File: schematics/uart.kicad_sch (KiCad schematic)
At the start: 8 parts, among them J8 myBus, U8 74HC238, U9 W65C51N, X1 CXO_DIP8

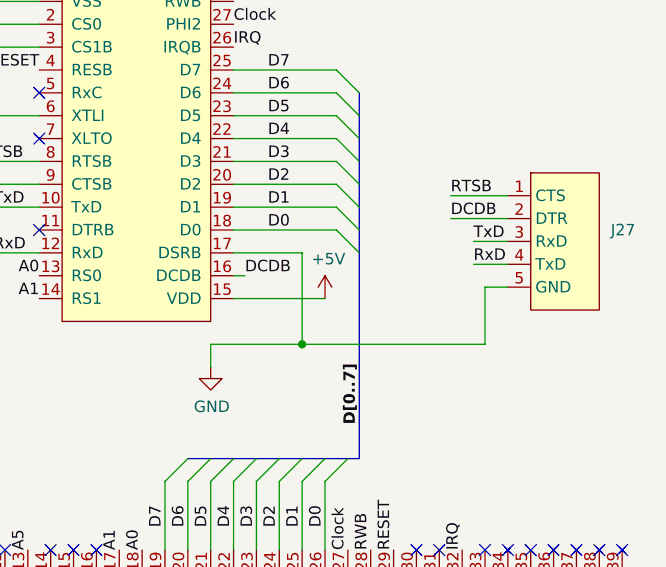
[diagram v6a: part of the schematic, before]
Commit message: new UART support
fix schematics by adding a resistor
renaming PC/2 to correct PS/2
Updating FORTH to detect terminal connection
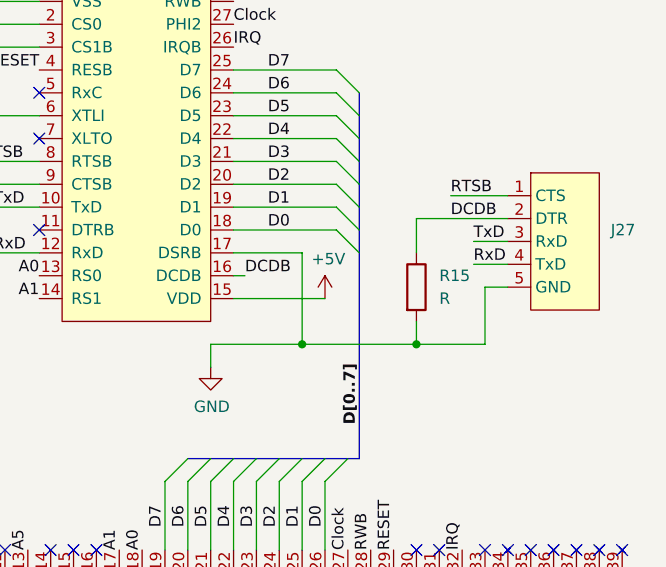
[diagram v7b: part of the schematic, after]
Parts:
- added R15: R, symbol Device:R
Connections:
- net DCDB: now also R15.1
- net GND: now also R15.2
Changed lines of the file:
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@@
+	)
+	(junction
+		(at 162.56 115.57)
+		(diameter 0)
+		(color 0 0 0 0)
 	)
 	(junction
@@
 		)
 	)
+	(wire
+		(pts
+			(xy 162.56 113.03) (xy 162.56 115.57)
+		)
+		(stroke
+			(width 0)
+			(type default)
+		)
+	)
 	(bus
 		(pts
@@
 	(wire
 		(pts
+			(xy 162.56 115.57) (xy 170.18 115.57)
+		)
+		(stroke
+			(width 0)
+			(type default)
+		)
+	)
+	(wire
+		(pts
 			(xy 142.24 100.33) (xy 153.67 100.33)
 		)
@@
 	(wire
 		(pts
+			(xy 162.56 101.6) (xy 172.72 101.6)
+		)
+		(stroke
+			(width 0)
+			(type default)
+		)
+	)
+	(wire
+		(pts
 			(xy 107.95 64.77) (xy 111.76 64.77)
 		)
@@
 	(wire
 		(pts
+			(xy 162.56 105.41) (xy 162.56 101.6)
+		)
+		(stroke
+			(width 0)
+			(type default)
+		)
+	)
+	(wire
+		(pts
 			(xy 100.33 105.41) (xy 100.33 100.33)
 		)
@@
 	(wire
 		(pts
-			(xy 166.37 101.6) (xy 172.72 101.6)
-		)
-		(stroke
-			(width 0)
-			(type default)
-		)
-	)
-	(wire
-		(pts
 			(xy 142.24 87.63) (xy 153.67 87.63)
 		)
@@
 	(wire
 		(pts
-			(xy 149.86 115.57) (xy 170.18 115.57)
+			(xy 149.86 115.57) (xy 162.56 115.57)
 		)
 		(stroke
@@
 					(unit 1)
 				)
+			)
+		)
+	)
+	(symbol
+		(lib_id "Device:R")
+		(at 162.56 109.22 0)
+		(unit 1)
+		(exclude_from_sim no)
+		(in_bom yes)
+		(on_board yes)
+		(dnp no)
+		(fields_autoplaced yes)
+		(property "Reference" "R15"
+			(at 165.1 107.9499 0)
+			(effects
+				(font
+					(size 1.27 1.27)
+				)
+				(justify left)
+			)
+		)
+		(property "Value" "R"
+			(at 165.1 110.4899 0)
+			(effects
+				(font
+					(size 1.27 1.27)
+				)
+				(justify left)
+			)
+		)
+		(property "Footprint" ""
+			(at 160.782 109.22 90)
+			(effects
+				(font
+					(size 1.27 1.27)
+				)
+				(hide yes)
+			)
+		)
+		(property "Datasheet" "~"
+			(at 162.56 109.22 0)
+			(effects
+				(font
+					(size 1.27 1.27)
+				)
+				(hide yes)
+			)
+		)
+		(property "Description" "Resistor"
+			(at 162.56 109.22 0)
+			(effects
+				(font
+					(size 1.27 1.27)
+				)
+				(hide yes)
+			)
+		)
+		(pin "2"
+		)
+		(pin "1"
+		)
+		(instances
+			(project ""
+				(path "/03a78ca6-eaff-4f05-be7b-36cd15f8b56d/e1937880-b4d5-4732-8378-398cc9358f14"
+					(reference "R15")
+					(unit 1)
+				)

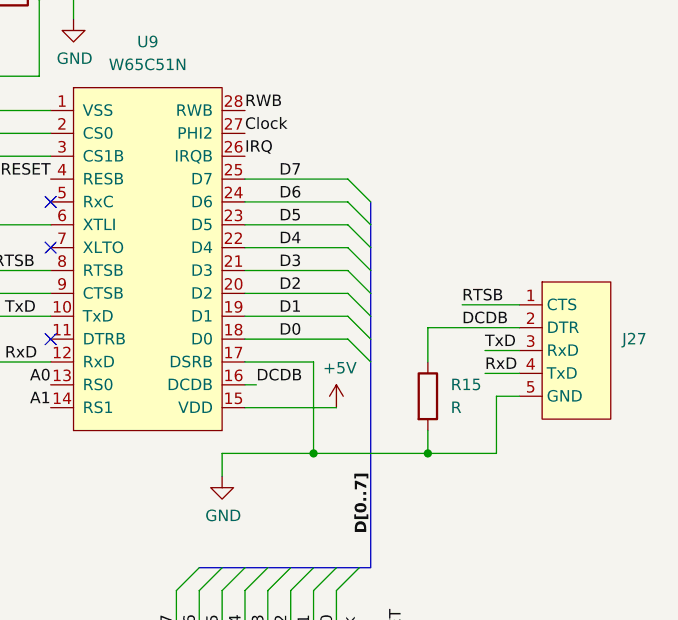
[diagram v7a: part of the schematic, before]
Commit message: Fix UART pullup
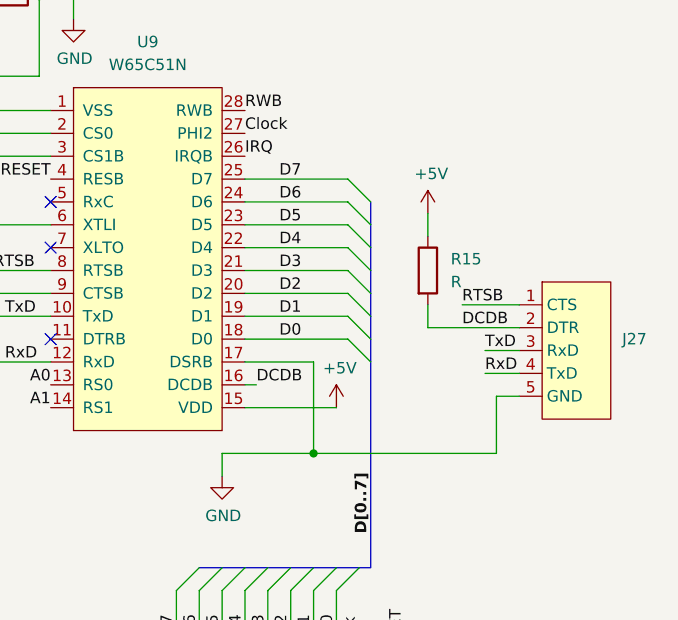
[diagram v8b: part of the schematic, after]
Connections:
- net +5V: now also R15.1
- net DCDB: now also R15.2; no longer R15.1
- net GND: no longer R15.2
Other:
- moved on the sheet: R15
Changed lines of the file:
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@@
-	)
-	(junction
-		(at 162.56 115.57)
-		(diameter 0)
-		(color 0 0 0 0)
 	)
 	(junction
@@
 		)
 	)
-	(wire
-		(pts
-			(xy 162.56 113.03) (xy 162.56 115.57)
-		)
-		(stroke
-			(width 0)
-			(type default)
-		)
-	)
 	(bus
 		(pts
@@
 	(wire
 		(pts
-			(xy 162.56 115.57) (xy 170.18 115.57)
+			(xy 149.86 115.57) (xy 170.18 115.57)
 		)
 		(stroke
@@
 	(wire
 		(pts
+			(xy 162.56 99.06) (xy 162.56 101.6)
+		)
+		(stroke
+			(width 0)
+			(type default)
+		)
+	)
+	(wire
+		(pts
 			(xy 113.03 82.55) (xy 120.65 82.55)
 		)
@@
 	(wire
 		(pts
+			(xy 162.56 88.9) (xy 162.56 91.44)
+		)
+		(stroke
+			(width 0)
+			(type default)
+		)
+	)
+	(wire
+		(pts
 			(xy 107.95 64.77) (xy 111.76 64.77)
 		)
@@
 	(wire
 		(pts
-			(xy 162.56 105.41) (xy 162.56 101.6)
-		)
-		(stroke
-			(width 0)
-			(type default)
-		)
-	)
-	(wire
-		(pts
 			(xy 100.33 105.41) (xy 100.33 100.33)
 		)
@@
 		(pts
 			(xy 68.58 57.15) (xy 68.58 59.69)
-		)
-		(stroke
-			(width 0)
-			(type default)
-		)
-	)
-	(wire
-		(pts
-			(xy 149.86 115.57) (xy 162.56 115.57)
 		)
 		(stroke
@@
 	)
 	(symbol
+		(lib_id "power:+5V")
+		(at 162.56 88.9 0)
+		(unit 1)
+		(exclude_from_sim no)
+		(in_bom yes)
+		(on_board yes)
+		(dnp no)
+		(property "Reference" "#PWR0132"
+			(at 162.56 92.71 0)
+			(effects
+				(font
+					(size 1.27 1.27)
+				)
+				(hide yes)
+			)
+		)
+		(property "Value" "+5V"
+			(at 162.941 84.5058 0)
+			(effects
+				(font
+					(size 1.27 1.27)
+				)
+			)
+		)
+		(property "Footprint" ""
+			(at 162.56 88.9 0)
+			(effects
+				(font
+					(size 1.27 1.27)
+				)
+				(hide yes)
+			)
+		)
+		(property "Datasheet" ""
+			(at 162.56 88.9 0)
+			(effects
+				(font
+					(size 1.27 1.27)
+				)
+				(hide yes)
+			)
+		)
+		(property "Description" "Power symbol creates a global label with name \"+5V\""
+			(at 162.56 88.9 0)
+			(effects
+				(font
+					(size 1.27 1.27)
+				)
+				(hide yes)
+			)
+		)
+		(pin "1"
+		)
+		(instances
+			(project "marcus"
+				(path "/03a78ca6-eaff-4f05-be7b-36cd15f8b56d/e1937880-b4d5-4732-8378-398cc9358f14"
+					(reference "#PWR0132")
+					(unit 1)
+				)
+			)
+		)
+	)
+	(symbol
 		(lib_id "Device:R")
-		(at 162.56 109.22 0)
+		(at 162.56 95.25 0)
 		(unit 1)
 		(exclude_from_sim no)
@@
 		(fields_autoplaced yes)
 		(property "Reference" "R15"
-			(at 165.1 107.9499 0)
+			(at 165.1 93.9799 0)
 			(effects
 				(font
@@
 		)
 		(property "Value" "R"
-			(at 165.1 110.4899 0)
+			(at 165.1 96.5199 0)
 			(effects
 				(font
@@
 		)
 		(property "Footprint" ""
-			(at 160.782 109.22 90)
+			(at 160.782 95.25 90)
 			(effects
 				(font
@@
 		)
 		(property "Datasheet" "~"
-			(at 162.56 109.22 0)
+			(at 162.56 95.25 0)
 			(effects
 				(font
@@
 		)
 		(property "Description" "Resistor"
-			(at 162.56 109.22 0)
-			(effects
-				(font
+			(at 162.56 95.25 0)
+			(effects
+				(font
